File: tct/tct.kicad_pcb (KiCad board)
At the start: 2 copper layers, 57.4 x 57.4 mm, 6 parts, among them IC1 ATTINY85-P, P1 CONN_01X02, U1 DIL40_IC

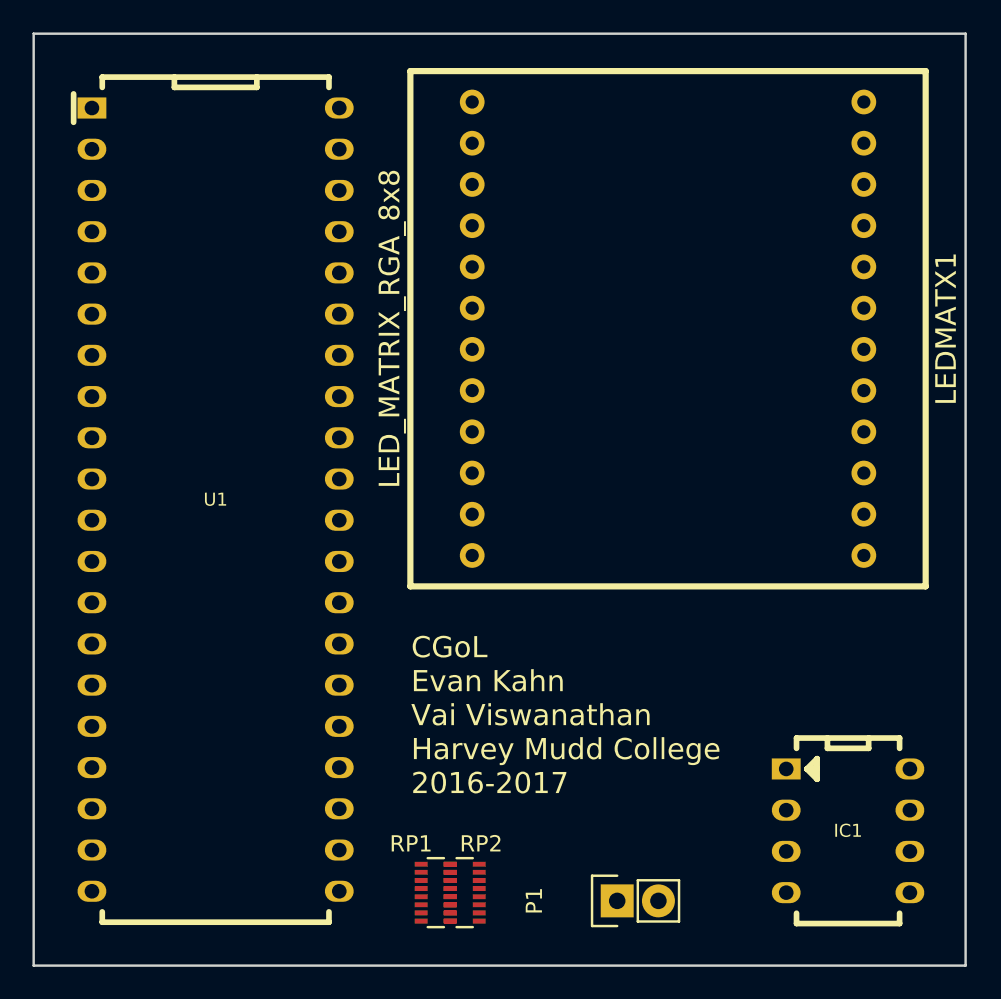
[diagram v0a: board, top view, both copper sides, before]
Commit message: PCB routing finished.
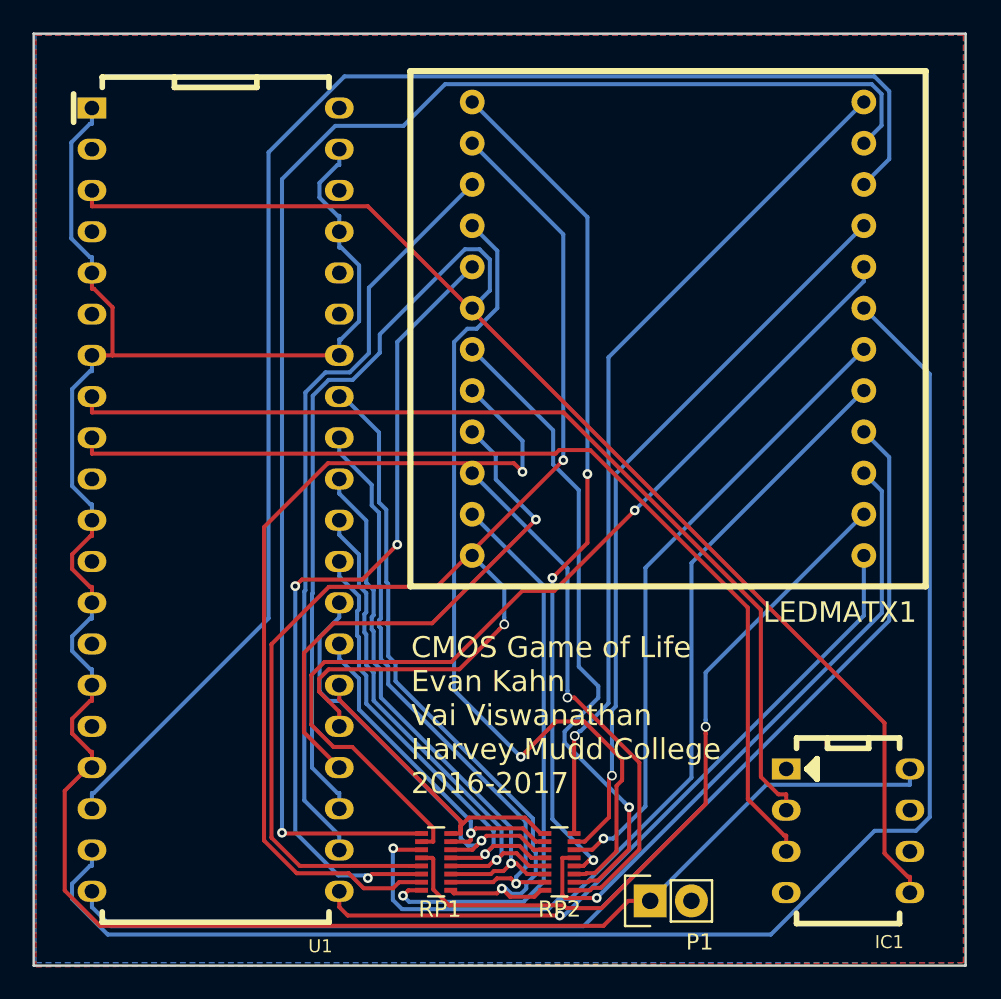
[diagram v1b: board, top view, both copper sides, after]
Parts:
- moved RP2 6.14 mm to (83.1, 96.2)
- moved P1 2.03 mm to (88.6, 98.6)
- moved RP1 1.89 mm to (75.5, 96.2)
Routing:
- net VCC: track 0.00 -> 143.3 mm
- net /r2: track 0.00 -> 93.4 mm
- net Net-(LEDMATX1-Pad23): track 0.00 -> 92.0 mm, vias 0 -> 1
- net /r1: track 0.00 -> 92.0 mm
- net /rst: track 0.00 -> 74.2 mm
- net /r3: track 0.00 -> 70.7 mm
- net Net-(LEDMATX1-Pad2): track 0.00 -> 66.4 mm, vias 0 -> 1
- net /ph2: track 0.00 -> 61.6 mm
- net /ph1: track 0.00 -> 60.5 mm
- net Net-(LEDMATX1-Pad20): track 0.00 -> 59.8 mm, vias 0 -> 1
- net Net-(LEDMATX1-Pad17): track 0.00 -> 55.2 mm, vias 0 -> 1
- net Net-(LEDMATX1-Pad8): track 0.00 -> 54.5 mm, vias 0 -> 1
- net Net-(LEDMATX1-Pad4): track 0.00 -> 53.6 mm, vias 0 -> 1
- net Net-(LEDMATX1-Pad1): track 0.00 -> 52.9 mm, vias 0 -> 3
- net Net-(LEDMATX1-Pad24): track 0.00 -> 52.5 mm, vias 0 -> 1
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- added copper zone on B.Cu, net GND
- added copper zone on F.Cu, net GND
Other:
- board text added: "CMOS Game of Life Evan Kahn Vai Viswanathan Harvey Mudd College 2016-2017"
- board text removed: "CGoL Evan Kahn Vai Viswanathan Harvey Mudd College 2016-2017"

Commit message: fixed layout with proper display pinout
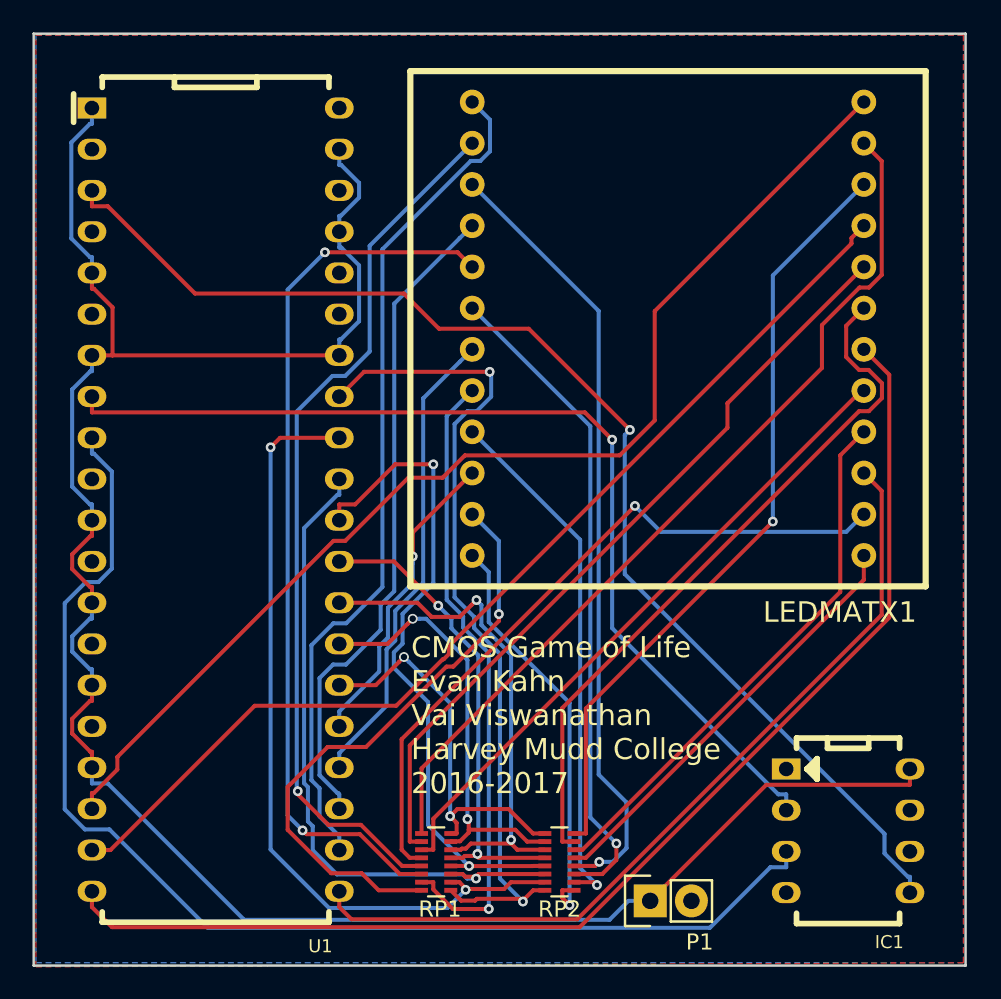
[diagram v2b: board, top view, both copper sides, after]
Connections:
- LEDMATX1 pad 1: Net-(LEDMATX1-Pad1) -> /r5
- LEDMATX1 pad 10: Net-(LEDMATX1-Pad10) -> /r8
- LEDMATX1 pad 12: /r8 -> Net-(LEDMATX1-Pad12)
- LEDMATX1 pad 13: /r4 -> Net-(LEDMATX1-Pad13)
- LEDMATX1 pad 15: Net-(LEDMATX1-Pad15) -> /r4
- LEDMATX1 pad 16: /r3 -> Net-(LEDMATX1-Pad16)
- LEDMATX1 pad 18: Net-(LEDMATX1-Pad18) -> /r3
- LEDMATX1 pad 19: /r2 -> Net-(LEDMATX1-Pad19)
- LEDMATX1 pad 21: Net-(LEDMATX1-Pad21) -> /r2
- LEDMATX1 pad 22: /r1 -> Net-(LEDMATX1-Pad22)
- LEDMATX1 pad 24: Net-(LEDMATX1-Pad24) -> /r1
- LEDMATX1 pad 3: /r5 -> Net-(LEDMATX1-Pad3)
- LEDMATX1 pad 4: Net-(LEDMATX1-Pad4) -> /r6
- LEDMATX1 pad 6: /r6 -> Net-(LEDMATX1-Pad6)
- LEDMATX1 pad 7: Net-(LEDMATX1-Pad7) -> /r7
- LEDMATX1 pad 9: /r7 -> Net-(LEDMATX1-Pad9)
- RP2 pad 10: Net-(LEDMATX1-Pad7) -> Net-(LEDMATX1-Pad9)
- RP2 pad 11: Net-(LEDMATX1-Pad4) -> Net-(LEDMATX1-Pad6)
- RP2 pad 12: Net-(LEDMATX1-Pad1) -> Net-(LEDMATX1-Pad3)
- RP2 pad 13: Net-(LEDMATX1-Pad15) -> Net-(LEDMATX1-Pad13)
- RP2 pad 14: Net-(LEDMATX1-Pad18) -> Net-(LEDMATX1-Pad16)
- RP2 pad 15: Net-(LEDMATX1-Pad21) -> Net-(LEDMATX1-Pad19)
- RP2 pad 16: Net-(LEDMATX1-Pad24) -> Net-(LEDMATX1-Pad22)
- RP2 pad 9: Net-(LEDMATX1-Pad10) -> Net-(LEDMATX1-Pad12)
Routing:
- net Net-(LEDMATX1-Pad4): track 53.6 -> 0.00 mm, vias 1 -> 0
- net Net-(LEDMATX1-Pad1): track 52.9 -> 0.00 mm, vias 3 -> 0
- net Net-(LEDMATX1-Pad24): track 52.5 -> 0.00 mm, vias 1 -> 0
- net Net-(LEDMATX1-Pad3): track 0.00 -> 48.5 mm, vias 0 -> 1
- net Net-(LEDMATX1-Pad22): track 0.00 -> 47.8 mm, vias 0 -> 1
- net Net-(LEDMATX1-Pad21): track 45.7 -> 0.00 mm, vias 1 -> 0
- net Net-(LEDMATX1-Pad19): track 0.00 -> 43.8 mm
- net Net-(LEDMATX1-Pad7): track 40.8 -> 0.00 mm, vias 1 -> 0
- net Net-(LEDMATX1-Pad6): track 0.00 -> 40.6 mm, vias 0 -> 1
- net Net-(LEDMATX1-Pad18): track 39.2 -> 0.00 mm, vias 1 -> 0
- net Net-(LEDMATX1-Pad15): track 39.1 -> 0.00 mm, vias 1 -> 0
- net Net-(LEDMATX1-Pad23): track 92.0 -> 55.1 mm, vias 1 -> 0
- net Net-(LEDMATX1-Pad16): track 0.00 -> 33.4 mm
- net Net-(LEDMATX1-Pad10): track 32.8 -> 0.00 mm, vias 1 -> 0
- net Net-(LEDMATX1-Pad9): track 0.00 -> 32.6 mm, vias 0 -> 1
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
